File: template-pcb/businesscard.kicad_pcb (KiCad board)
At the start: 2 copper layers, 85 x 55 mm, 40 parts, among them J1 USB_B_Micro, U1 NE555, U2 4017

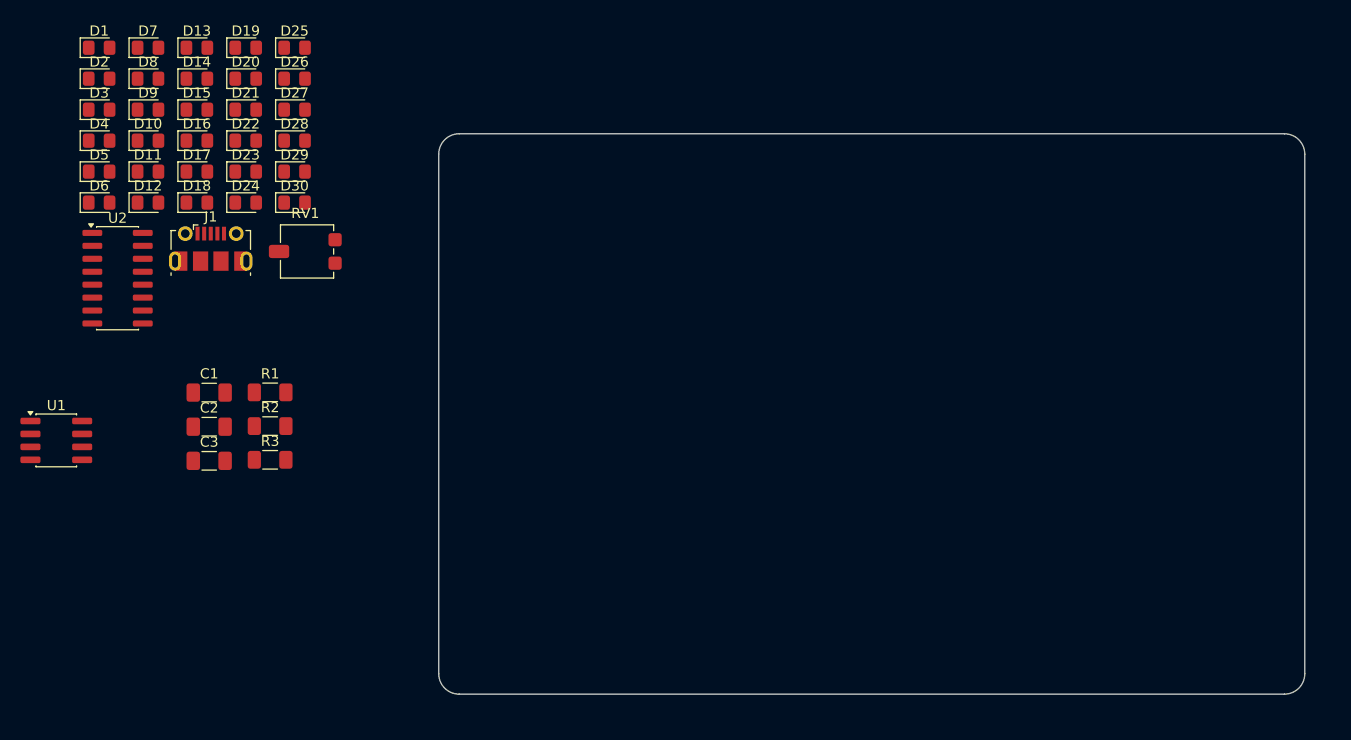
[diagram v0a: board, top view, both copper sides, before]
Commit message: layouting and routing of leds
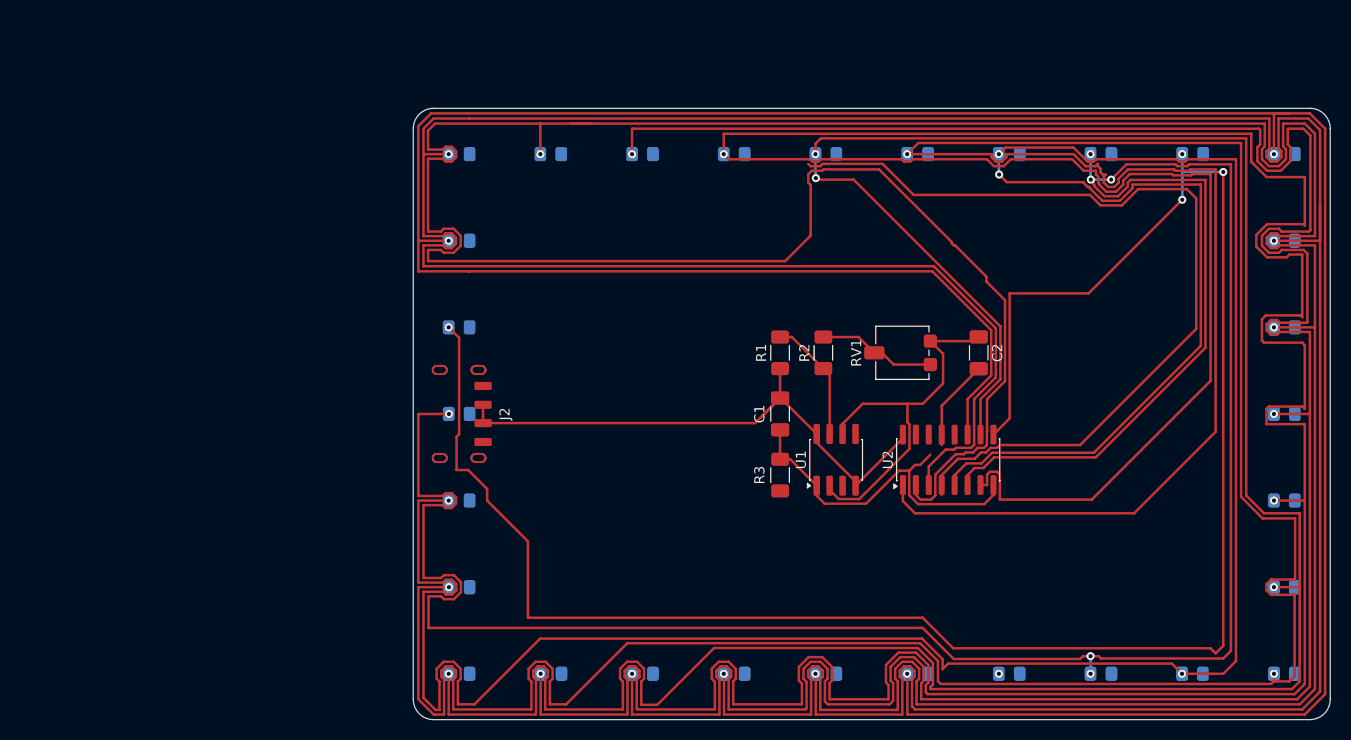
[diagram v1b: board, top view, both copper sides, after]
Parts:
- removed C3: CP_Small, Capacitor_SMD:C_1206_3216Metric_Pad1.33x1.80mm_HandSolder
- removed J1: USB_B_Micro, Connector_USB:USB_Micro-B_Molex-105017-0001
- added J2: USB_C_Receptacle_PowerOnly_4P, usb-c:usb-c-4-pins, F.Cu at (112.5, 102.5)
- C1, C2: value CAP -> 1uf
- D1, D10, D11, D12, D13, D14, D15, D16, D17, D18, D19, D2, D20, D21, D22, D23, D24, D25, D26, D27, D28, D29, D3, D30, D4, D5, D6, D7, D8, D9: moved to B.Cu
- R1: value R -> 2k
- R2: value R -> 10k
- R3: value R -> 1k
- RV1: value R_POT -> 50k
- U2: value 4017 -> CD4017
- moved D6 125.2 mm to (198.0, 128.0), turned to 180 degrees
- moved D5 123.3 mm to (198.0, 119.5), turned to 180 degrees
- moved D4 121.6 mm to (198.0, 111.0), turned to 180 degrees
- moved D3 120.1 mm to (198.0, 102.5), turned to 180 degrees
- moved D7 119.5 mm to (189.0, 128.0), turned to 180 degrees
- moved D2 118.9 mm to (198.0, 94.0), turned to 180 degrees
- moved D1 117.9 mm to (198.0, 85.5), turned to 180 degrees
- moved D8 110.3 mm to (180.0, 128.0), turned to 180 degrees
- moved D9 101.1 mm to (171.0, 128.0), turned to 180 degrees
- moved D30 97.3 mm to (198.0, 77.0), turned to 180 degrees
- moved D10 91.9 mm to (162.0, 128.0), turned to 180 degrees
- moved D29 88.2 mm to (189.0, 77.0), turned to 180 degrees
- moved U2 83.5 mm to (165.0, 107.0), turned to 90 degrees
- moved D11 82.8 mm to (153.0, 128.0), turned to 180 degrees
- moved D28 79.2 mm to (180.0, 77.0), turned to 180 degrees
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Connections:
- net Net-(D1-A) renamed Q0
- net Net-(D10-A) renamed Q9
- net Net-(D12-A) renamed Q1
- net Net-(D13-A) renamed Q2
- net Net-(D14-A) renamed Q3
- net Net-(D15-A) renamed Q4
- net Net-(D16-A) renamed Q5
- net Net-(D17-A) renamed Q6
- net Net-(D19-A) renamed Q8
- net Net-(J1-VBUS) renamed +5V
- net Net-(U1-DIS) renamed DISCH
- net Net-(U1-Q) renamed CLK
- C1 pad 2: Net-(J1-GND) -> GND
- C2 pad 1: Net-(U1-CV) -> TRIG/TRSH
- C2 pad 2: Net-(J1-GND) -> GND
- D1 pad 1: Net-(D1-K) -> LED_GND
- D10 pad 1: Net-(D1-K) -> LED_GND
- D11 pad 1: Net-(D1-K) -> LED_GND
- D12 pad 1: Net-(D1-K) -> LED_GND
- D13 pad 1: Net-(D1-K) -> LED_GND
- D14 pad 1: Net-(D1-K) -> LED_GND
- D15 pad 1: Net-(D1-K) -> LED_GND
- D16 pad 1: Net-(D1-K) -> LED_GND
- D17 pad 1: Net-(D1-K) -> LED_GND
- D18 pad 1: Net-(D1-K) -> LED_GND
- D18 pad 2: Net-(D18-A) -> Q7
- D19 pad 1: Net-(D1-K) -> LED_GND
- D2 pad 1: Net-(D1-K) -> LED_GND
- D20 pad 1: Net-(D1-K) -> LED_GND
- D21 pad 1: Net-(D1-K) -> LED_GND
- D22 pad 1: Net-(D1-K) -> LED_GND
- D23 pad 1: Net-(D1-K) -> LED_GND
- D24 pad 1: Net-(D1-K) -> LED_GND
- D25 pad 1: Net-(D1-K) -> LED_GND
- D26 pad 1: Net-(D1-K) -> LED_GND
- D27 pad 1: Net-(D1-K) -> LED_GND
- D28 pad 1: Net-(D1-K) -> LED_GND
- D28 pad 2: unconnected-(D28-A-Pad2) -> Q7
- D29 pad 1: Net-(D1-K) -> LED_GND
- D3 pad 1: Net-(D1-K) -> LED_GND
- D30 pad 1: Net-(D1-K) -> LED_GND
- D4 pad 1: Net-(D1-K) -> LED_GND
- D5 pad 1: Net-(D1-K) -> LED_GND
- D6 pad 1: Net-(D1-K) -> LED_GND
- D7 pad 1: Net-(D1-K) -> LED_GND
- D8 pad 1: Net-(D1-K) -> LED_GND
- D8 pad 2: Net-(D18-A) -> Q7
- D9 pad 1: Net-(D1-K) -> LED_GND
- R3 pad 1: Net-(D1-K) -> GND
- R3 pad 2: Net-(J1-GND) -> LED_GND
- RV1 pad 1: Net-(U1-TR) -> TRIG/TRSH
- U1 pad 1: Net-(J1-GND) -> GND
- U1 pad 2: Net-(U1-TR) -> TRIG/TRSH
- U1 pad 5: Net-(U1-CV) -> unconnected-(U1-CV-Pad5)
- U1 pad 6: Net-(U1-THR) -> TRIG/TRSH
- U2 pad 13: Net-(J1-GND) -> GND
- U2 pad 15: Net-(J1-GND) -> GND
- U2 pad 6: Net-(D18-A) -> Q7
- U2 pad 8: Net-(J1-GND) -> GND
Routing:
- net Q1: track 0.00 -> 371.4 mm, vias 0 -> 3
- net Q3: track 0.00 -> 356.3 mm, vias 0 -> 3
- net Q2: track 0.00 -> 335.8 mm, vias 0 -> 3
- net Q0: track 0.00 -> 324.8 mm, vias 0 -> 3
- net Q5: track 0.00 -> 316.4 mm, vias 0 -> 3
- net Q9: track 0.00 -> 284.1 mm, vias 0 -> 3
- net Q6: track 0.00 -> 268.0 mm, vias 0 -> 4
- net Q4: track 0.00 -> 253.2 mm, vias 0 -> 4
- net Q7: track 0.00 -> 244.0 mm, vias 0 -> 6
- net Q8: track 0.00 -> 193.0 mm, vias 0 -> 5
- net +5V: track 0.00 -> 56.8 mm
- net GND: track 0.00 -> 46.2 mm
- net TRIG/TRSH: track 0.00 -> 37.3 mm
- net DISCH: track 0.00 -> 12.2 mm
- net Net-(R2-Pad2): track 0.00 -> 11.6 mm
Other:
- board size 85 x 55 mm -> 90 x 60 mm
- board text added: "${REFERENCE}"
- board text added: "PCB EDGE"

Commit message: finishing routing and erc
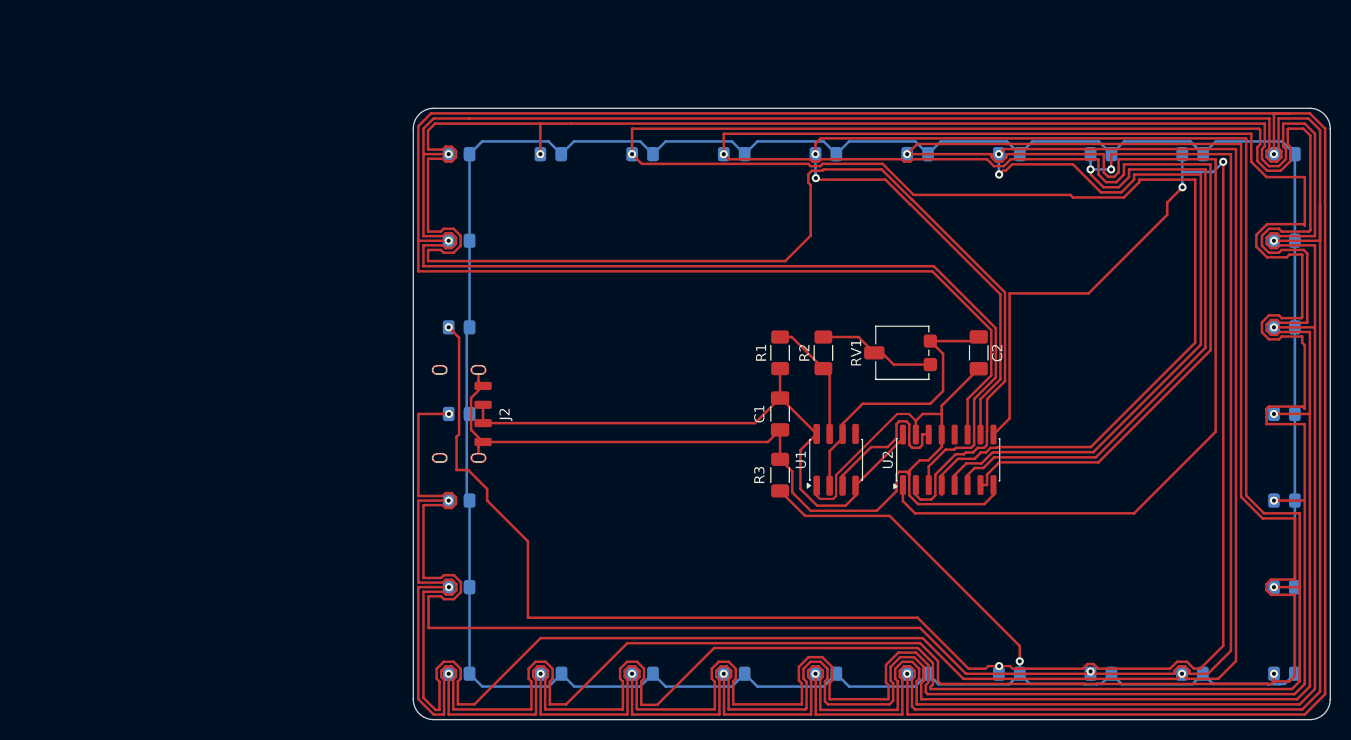
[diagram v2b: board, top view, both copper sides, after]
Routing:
- net LED_GND: track 0.00 -> 314.9 mm, vias 0 -> 1
- net GND: track 46.2 -> 108.2 mm
- net Q2: track 335.8 -> 355.5 mm
- net CLK: track 0.00 -> 15.9 mm
- net TRIG/TRSH: track 37.3 -> 28.1 mm
- net +5V: track 56.8 -> 61.7 mm
- net Q8: track 193.0 -> 197.6 mm, vias 5 -> 4
- net Q3: track 356.3 -> 351.9 mm
- net Q7: track 244.0 -> 247.7 mm, vias 6 -> 4
- net Q1: track 371.4 -> 369.5 mm
- net Q4: track 253.2 -> 255.0 mm
- net Q6: track 268.0 -> 269.4 mm
- net Q5: track 316.4 -> 317.0 mm
